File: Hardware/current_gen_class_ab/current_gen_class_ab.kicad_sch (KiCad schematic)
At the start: 60 parts, among them J1 Conn_Coaxial, J2 Conn_Coaxial, J3 Conn_01x01_Socket, J4 Conn_01x01_Socket, J5 Conn_01x01_Socket, Q1 PMOS, Q2 NMOS, Q3 NMOS, Q4 PMOS, U1 Opamp_Dual, U2 Opamp_Dual

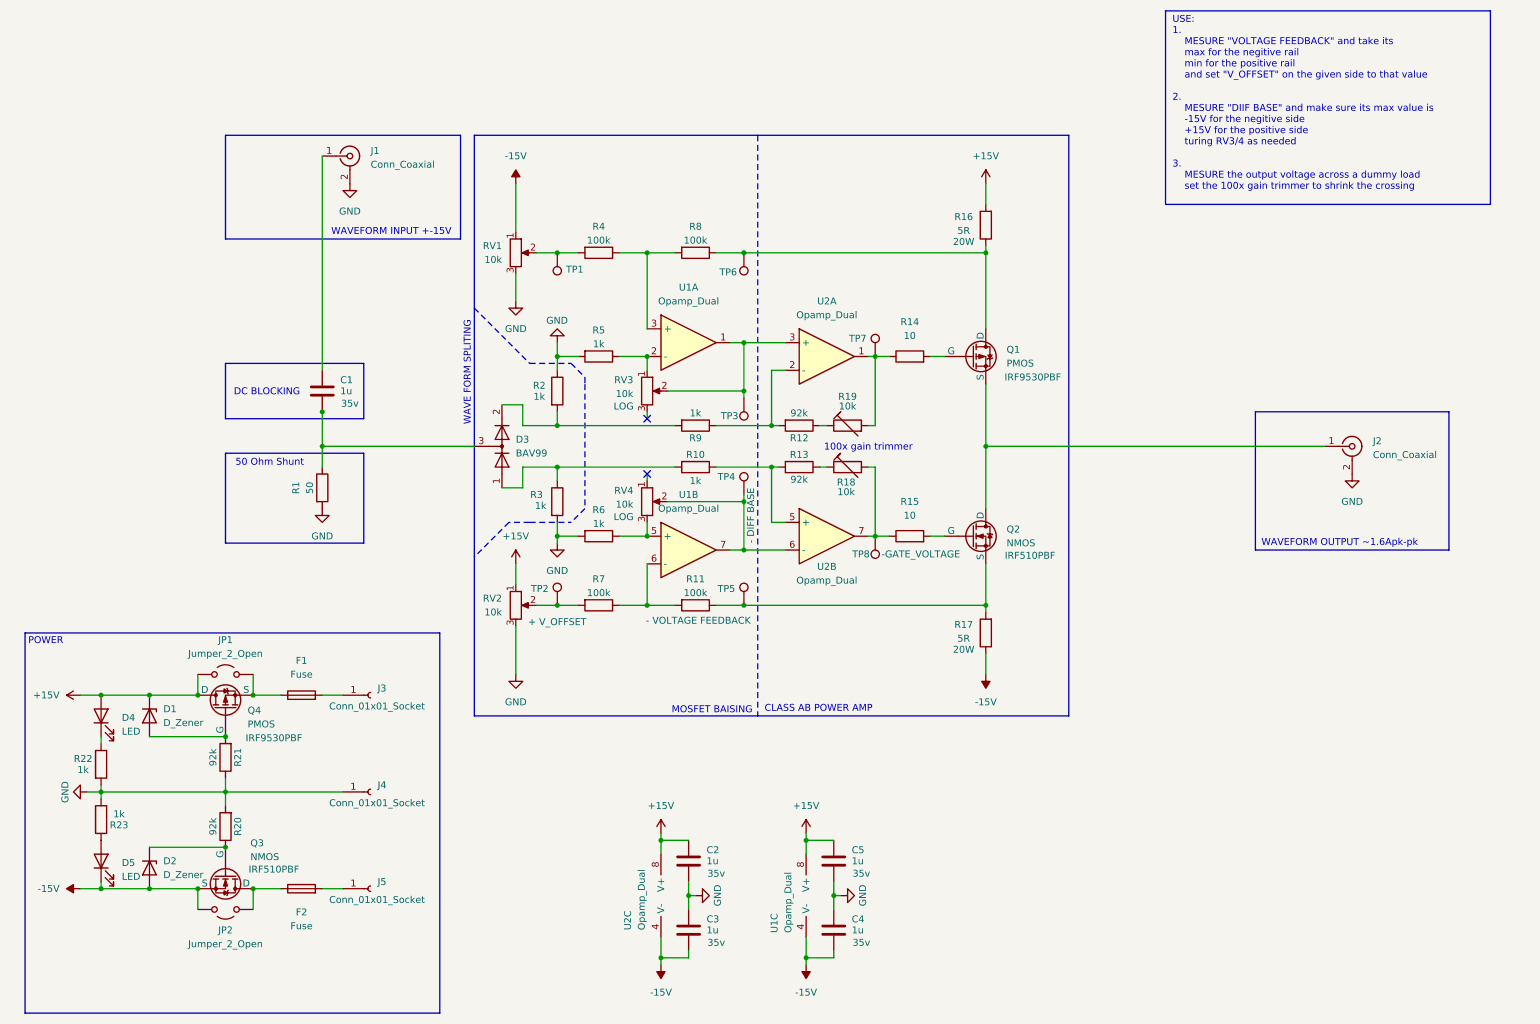
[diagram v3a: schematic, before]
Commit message: swapped pins around to suit pcb better
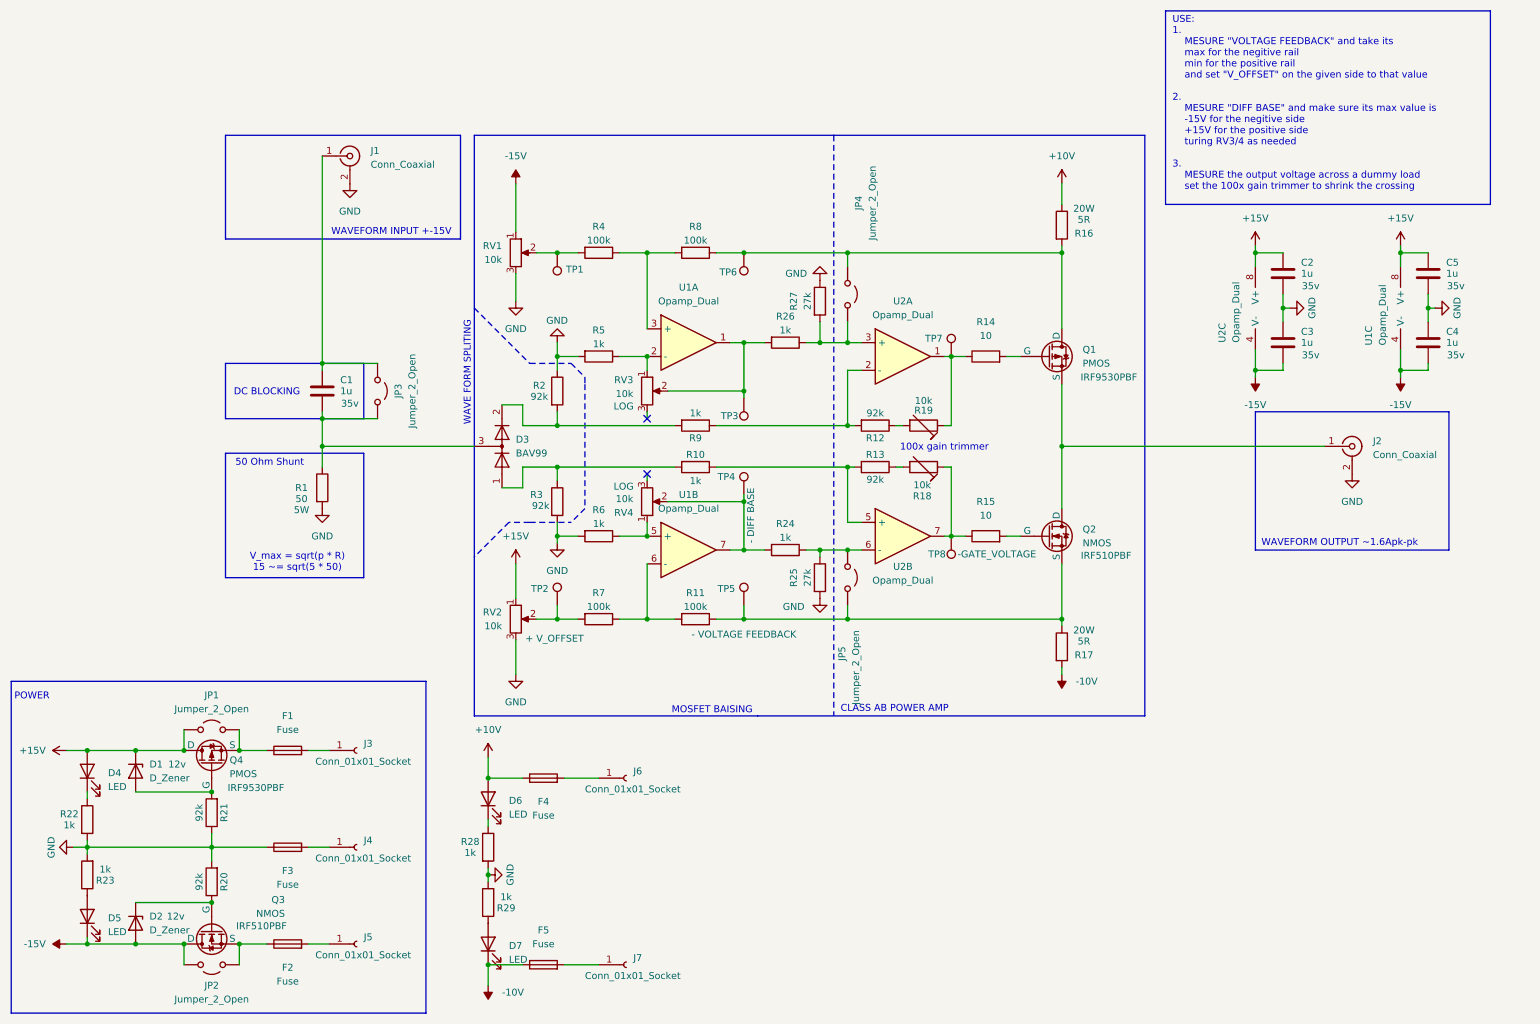
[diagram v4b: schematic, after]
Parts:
- added D6, D7: LED, Diode_SMD:D_0603_1608Metric, symbol Device:LED
- added F3, F4, F5: Fuse, Fuse:Fuseholder_Clip-5x20mm_Bel_FC-203-22_Lateral_P17.80x5.00mm_D1.17mm_Horizontal, symbol Device:Fuse
- added J6, J7: Conn_01x01_Socket, Connector:Banana_Jack_1Pin, symbol Connector:Conn_01x01_Socket
- added JP3, JP4, JP5: Jumper_2_Open, Jumper:SolderJumper-2_P1.3mm_Open_TrianglePad1.0x1.5mm, symbol Jumper:Jumper_2_Open
- added R24, R26, R28, R29: 1k, Resistor_SMD:R_0603_1608Metric, symbol Device:R
- added R25, R27: 27k, Resistor_SMD:R_0603_1608Metric, symbol Device:R
- C1, C2, C3, C4, C5: footprint (none) -> Capacitor_SMD:C_0805_2012Metric; Manufactor Number (none) -> CC0805KKX7R9BB105; Supplier Link (none) -> https://www.digikey.co.nz/en/products/detail/yageo/CC0805KK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
- D1, D2: footprint (none) -> Diode_SMD:D_SOD-123; Manufactor Number (none) -> MMSZ5231B-7-F; Notes (none) -> 12v; Supplier Link (none) -> https://www.diodes.com/assets/Datasheets/ds18015.pdf
- D4, D5: footprint (none) -> Diode_SMD:D_0603_1608Metric
- JP1, JP2: footprint (none) -> Jumper:SolderJumper-2_P1.3mm_Open_TrianglePad1.0x1.5mm
- R1: footprint (none) -> Resistor_THT:R_Axial_DIN0309_L9.0mm_D3.2mm_P12.70mm_Horizontal; Manufactor Number (none) -> UB5C-10RF1; Notes (none) -> 5W; Supplier Link (none) -> https://www.digikey.co.nz/en/products/detail/riedon-product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
- R10, R11, R12, R13, R14, R15, R20, R21, R22, R23, R4, R5, R6, R7, R8, R9: footprint (none) -> Resistor_SMD:R_0603_1608Metric
- R16, R17: footprint (none) -> Package_TO_SOT_THT:TO-220-2_Horizontal_TabDown
- R2, R3: value 1k -> 92k; footprint (none) -> Resistor_SMD:R_0603_1608Metric
- TP1, TP2, TP3, TP4, TP5, TP6, TP7, TP8: footprint (none) -> TestPoint:TestPoint_Bridge_Pitch2.54mm_Drill1.3mm
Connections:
- net +15V: no longer R16.2
- net -15V: now also Q3.1 (D); no longer Q3.3 (S), R17.1
- net GND: now also F3.1, R25.2, R27.1, R28.2, R29.2; no longer J4.1 (Pin_1)
- net at RV4.1: now also R6.1, U1.5 (+)
- net at RV4.2, TP4.1, U1.7: now also R24.2; no longer U2.6 (-)
- net at Q1.1 (D), R8.1, TP6.1: now also R16.2, JP4.1 (A); no longer R16.1
- net at R14.1, TP7.1, U2.1: now also R19.1; no longer R19.2
- net at F2.1, JP2.1 (A): now also Q3.3 (S); no longer Q3.1 (D)
- net at RV3.2, TP3.1, U1.1: now also R26.2; no longer U2.3 (+)
- net at R18.1: now also R15.1, TP8.1, U2.7; no longer R13.1
- net at Q2.3 (S), R11.1, TP5.1: now also R17.1, JP5.2 (B); no longer R17.2
- net at C1.1, D3.3 (K), R1.1: now also JP3.2 (B)
- net at C1.2: now also J1.1 (In), JP3.1 (A)
- net at R12.1: now also R19.2; no longer R19.1
- new net: F4.2, J6.1 (Pin_1)
- new net: JP5.1 (A), R24.1, R25.1, U2.6 (-)
- new net: D6.1 (K), R28.1
- new net: JP4.2 (B), R26.1, R27.2, U2.3 (+)
- new net: R13.1, R18.2
- new net: F5.2, J7.1 (Pin_1)
- new net: D7.2 (A), R29.1
- new net: F3.2, J4.1 (Pin_1)
- new net +10V: D6.2 (A), F4.1, R16.1
- new net -10V: D7.1 (K), F5.1, R17.2
- now unconnected: RV4.3
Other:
- note added: "USE: 1. MESURE "VOLTAGE FEEDBACK" and take its max for the negitive rail min for the positive rail and set "V_OFFSET" on the given side to that value 2. MESURE "DIFF BASE" and make sure its max value is -15V for the negitive side +15V for the positive side turing RV3/4 as needed 3. MESURE the output voltage across a dummy load set the 100x gain trimmer to shrink the crossing"
- note added: "V_max = sqrt(p * R) 15 ~= sqrt(5 * 50)"
- note removed: "USE: 1. MESURE "VOLTAGE FEEDBACK" and take its max for the negitive rail min for the positive rail and set "V_OFFSET" on the given side to that value 2. MESURE "DIIF BASE" and make sure its max value is -15V for the negitive side +15V for the positive side turing RV3/4 as needed 3. MESURE the output voltage across a dummy load set the 100x gain trimmer to shrink the crossing"
- moved on the sheet: C2, D1, D2, D4, D5, F1, F2, J3, J4, J5, JP1, JP2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

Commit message: updated 50ohm shunt
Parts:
- removed F3: Fuse, Fuse:Fuseholder_Clip-5x20mm_Bel_FC-203-22_Lateral_P17.80x5.00mm_D1.17mm_Horizontal, symbol Device:Fuse
- added H1, H2, H3, H4: MountingHole_Pad, MountingHole:MountingHole_3.2mm_M3_DIN965_Pad, symbol Mechanical:MountingHole_Pad
- R1: Manufactor Number UB5C-10RF1 -> AC05000005009JAC00; Supplier Link https://www.digikey.co.nz/en/products/detail/riedon-product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 -> https://www.digikey.co.nz/en/products/detail/vishay-beyschl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
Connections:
- net GND: now also J4.1 (Pin_1), U1.9 (thermal), U2.9 (thermal)
- no-connect marks 2 -> 6

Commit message: added more to BOM
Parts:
- C5: Supplier link (none) -> https://www.digikey.co.nz/en/products/detail/kemet/C0805C10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
- D3: Manufactor Part Number (none) -> BAV99; Supplier Part Number (none) -> BAV99; Supplier link (none) -> https://www.digikey.co.nz/en/products/detail/smc-diode-solu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
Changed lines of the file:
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@@
 			)
 		)
+		(property "Supplier Part Number" ""
+			(at 273.05 60.96 0)
+			(effects
+				(font
+					(size 1.27 1.27)
+				)
+				(hide yes)
+			)
+		)
+		(property "Supplier link" "https://www.digikey.co.nz/en/products/detail/kemet/C0805C105K6RACTU/7382122"
+			(at 273.05 60.96 0)
+			(effects
+				(font
+					(size 1.27 1.27)
+				)
+				(hide yes)
+			)
+		)
+		(property "Manufactor Part Number" ""
+			(at 273.05 60.96 0)
+			(effects
+				(font
+					(size 1.27 1.27)
+				)
+				(hide yes)
+			)
+		)
 		(pin "2"
 		)
@@
 		(dnp no)
 		(property "Reference" "JP4"
-			(at 168.402 48.006 0)
+			(at 170.434 64.008 0)
 			(effects
 				(font
@@
 		)
 		(property "Value" "Jumper_2_Open"
-			(at 170.942 48.006 0)
+			(at 172.974 64.008 0)
 			(effects
 				(font
@@
 			(at 102.87 92.71 0)
 			(effects
+				(font
+					(size 1.27 1.27)
+				)
+				(hide yes)
+			)
+		)
+		(property "Supplier Part Number" "BAV99"
+			(at 102.87 92.71 0)
+			(effects
+				(font
+					(size 1.27 1.27)
+				)
+				(hide yes)
+			)
+		)
+		(property "Supplier link" "https://www.digikey.co.nz/en/products/detail/smc-diode-solutions/BAV99/6022507"
+			(at 102.87 92.71 0)
+			(effects
+				(font
+					(size 1.27 1.27)
+				)
+				(hide yes)
+			)
+		)
+		(property "Notes" ""
+			(at 102.87 92.71 0)
+			(effects
+				(font
+					(size 1.27 1.27)
+				)
+				(hide yes)
+			)
+		)
+		(property "Manufactor Part Number" "BAV99"
+			(at 102.87 92.71 0)
+			(effects
